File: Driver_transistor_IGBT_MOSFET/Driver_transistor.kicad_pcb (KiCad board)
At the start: 2 copper layers, 79.5 x 34.3 mm, 12 parts, among them J3 Conn_01x02, J4 Conn_01x02, J5 Conn_01x01, Q5 IRF830, Q6 IRF830, Q7 IRG4BC30, T1 1:1

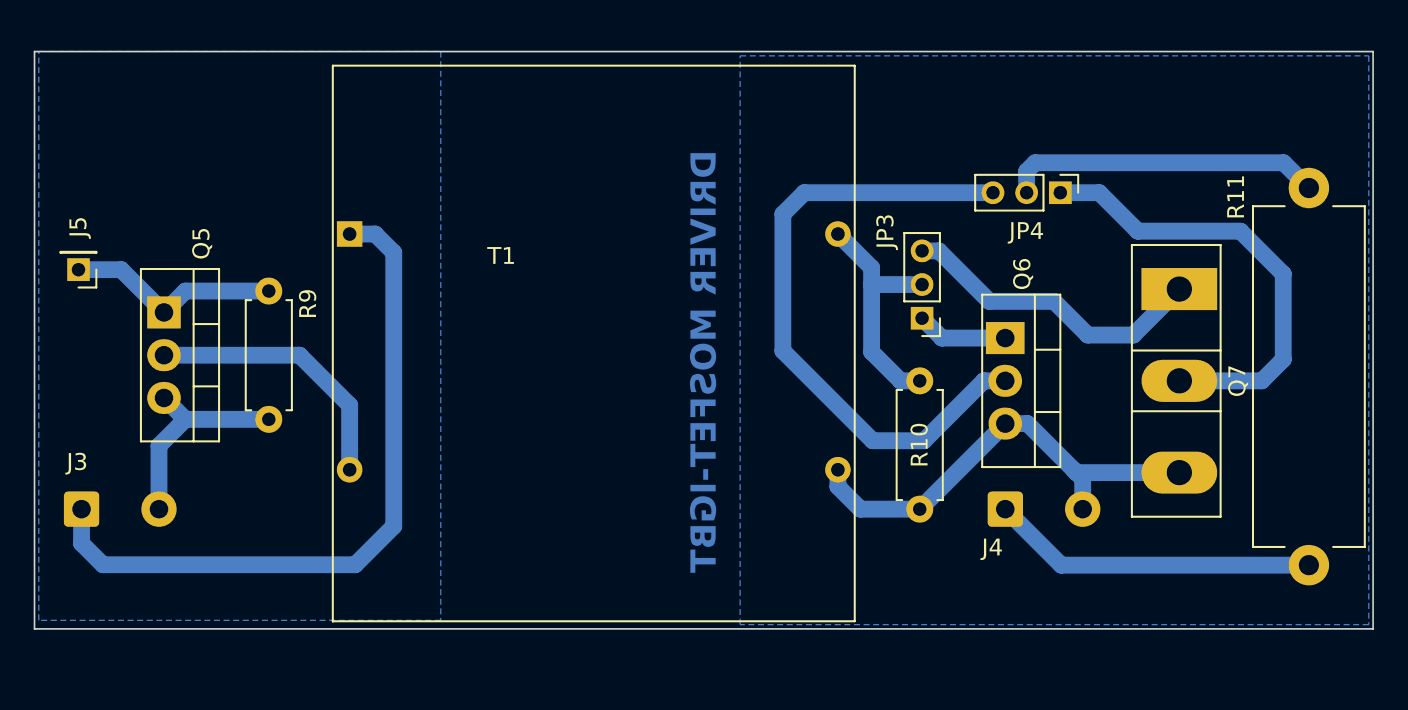
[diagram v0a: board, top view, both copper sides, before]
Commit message: rediseño driver IGBT-MOSFET
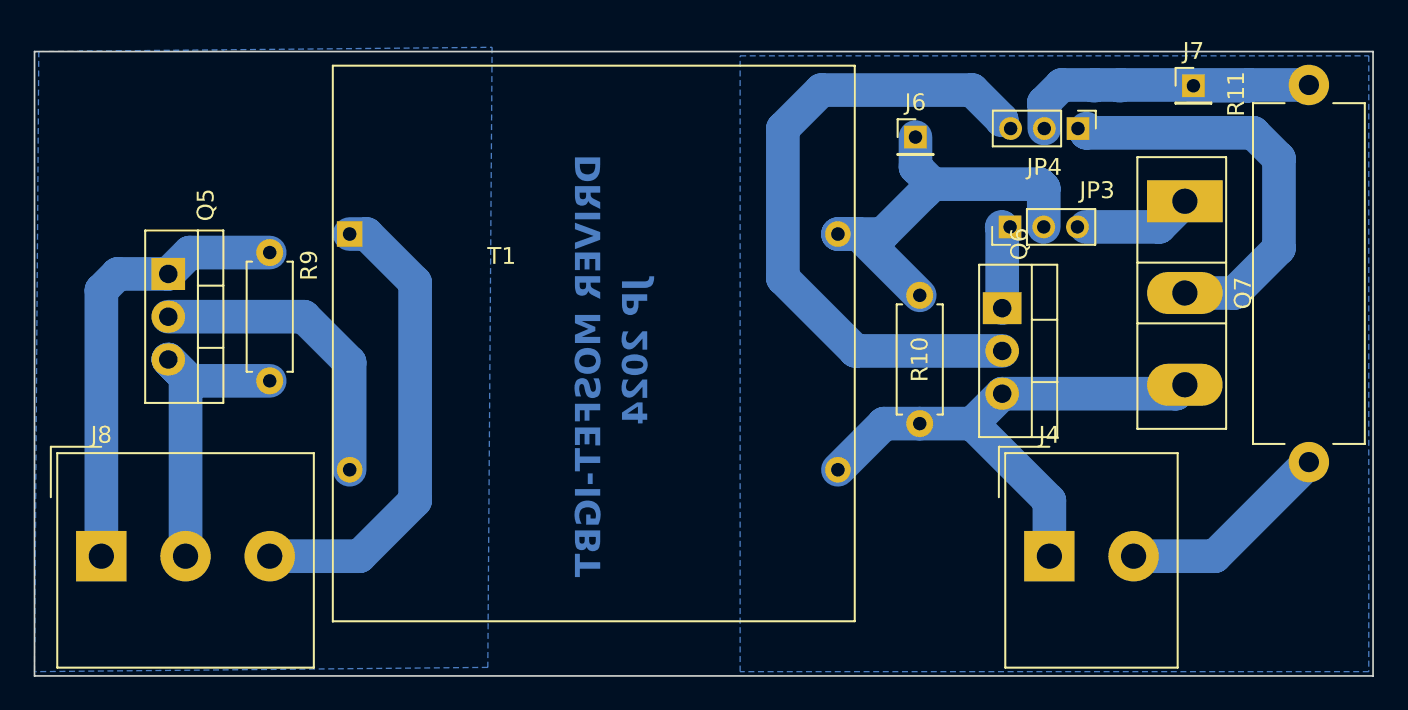
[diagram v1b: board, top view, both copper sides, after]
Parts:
- removed J3: Conn_01x02, Connector_Wire:SolderWire-0.5sqmm_1x02_P4.6mm_D0.9mm_OD2.1mm
- removed J5: Conn_01x01, Connector_PinHeader_2.00mm:PinHeader_1x01_P2.00mm_Vertical
- added J6: gate, Connector_PinHeader_2.00mm:PinHeader_1x01_P2.00mm_Vertical, F.Cu at (149.6, 31.2)
- added J7: drenador, Connector_PinHeader_2.00mm:PinHeader_1x01_P2.00mm_Vertical, F.Cu at (166.1, 28.2)
- added J8: Conn_01x03, TerminalBlock_Altech:Altech_AK300_1x03_P5.00mm_45-Degree, F.Cu at (101.3, 56.1)
- J4: footprint Connector_Wire:SolderWire-0.5sqmm_1x02_P4.6mm_D0.9mm_OD2.1mm -> TerminalBlock_Altech:Altech_AK300_1x02_P5.00mm_45-Degree
- moved JP3 7.53 mm to (155.2, 36.6), turned to 90 degrees
- moved R11 6.12 mm to (173.0, 28.1)
- moved Q7 5.23 mm to (165.6, 35.1)
- moved R10 5.08 mm to (149.9, 48.3)
- moved JP4 3.95 mm to (159.3, 30.7)
- moved J4 3.83 mm to (157.6, 56.1)
- moved Q5 2.30 mm to (105.2, 39.4)
- moved R9 2.29 mm to (111.3, 45.7)
- moved Q6 1.79 mm to (154.8, 41.4)
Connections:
- J4 pad 1: VDD -> GND2
- J4 pad 2: GND2 -> VDD
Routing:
- net pwm1: track 12.9 -> 26.7 mm
- net VCC: track 41.4 -> 28.0 mm
- net Net-(JP3-B): track 18.5 -> 6.51 mm
- net Net-(J6-Pin_1): track 14.4 -> 26.1 mm
- net VDD: track 19.4 -> 12.7 mm
- net GND1: track 12.7 -> 18.7 mm
- net GND2: track 27.5 -> 32.5 mm
- net Net-(JP4-A): track 27.0 -> 24.3 mm
- net Net-(J7-Pin_1): track 18.9 -> 21.2 mm
- net Net-(Q5-D): track 16.1 -> 18.3 mm
- net Net-(JP3-A): track 5.43 -> 4.84 mm
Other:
- board size 79.5 x 34.3 mm -> 79.5 x 37.1 mm
- board text added: "JP 2024"

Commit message: rediseño driver IGBT-MOSFET
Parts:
- moved R11 7.73 mm to (178.3, 33.7)
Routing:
- net Net-(J7-Pin_1): track 21.2 -> 30.6 mm
- net VDD: track 12.7 -> 15.7 mm
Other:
- board size 79.5 x 37.1 mm -> 85.9 x 37.1 mm
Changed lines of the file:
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@@
   )
   (footprint "Resistor_THT:R_Axial_Power_L20.0mm_W6.4mm_P22.40mm" (layer "F.Cu")
-    (at 172.974 28.146 -90)
+    (at 178.308 33.734 -90)
     (descr "Resistor, Axial_Power series, Box, pin pitch=22.4mm, 4W, length*width*height=20*6.4*6.4mm^3, http://cdn-reichelt.de/documents/datenblatt/B400/5WAXIAL_9WAXIAL_11WAXIAL_17WAXIAL%23YAG.pdf")
     (tags "Resistor Axial_Power series Box pin pitch 22.4mm 4W length 20mm width 6.4mm height 6.4mm")
@@
     )
   )
-  (gr_rect (start 97.282 26.162) (end 176.784 63.246)
+  (gr_rect (start 97.282 26.162) (end 183.134 63.246)
     (stroke (width 0.1) (type default)) (fill none) (layer "Edge.Cuts"))
   (gr_text "JP 2024" (at 133.858 39.624 90) (layer "B.Cu")
@@
   (segment (start 111.252 45.72) (end 106.497 45.72) (width 2) (layer "B.Cu") (net 2))
   (segment (start 106.497 45.72) (end 105.227 44.45) (width 2) (layer "B.Cu") (net 2))
-  (segment (start 162.56 56.134) (end 167.386 56.134) (width 2) (layer "B.Cu") (net 3))
-  (segment (start 167.386 56.134) (end 172.974 50.546) (width 2) (layer "B.Cu") (net 3))
+  (segment (start 178.308 56.134) (end 162.56 56.134) (width 2) (layer "B.Cu") (net 3))
   (segment (start 152.979 48.26) (end 154.757 46.482) (width 2) (layer "B.Cu") (net 4))
   (segment (start 157.56 56.134) (end 157.56 52.841) (width 2) (layer "B.Cu") (net 4))
@@
   (segment (start 145 37) (end 147.658 37) (width 2) (layer "B.Cu") (net 11))
   (segment (start 169.418 28.146) (end 161.798 28.146) (width 2) (layer "B.Cu") (net 12))
+  (segment (start 175.72 28.146) (end 178.308 30.734) (width 2) (layer "B.Cu") (net 12))
   (segment (start 166.116 28.194) (end 169.37 28.194) (width 2) (layer "B.Cu") (net 12))
   (segment (start 158.29 28.146) (end 157.226 29.21) (width 2) (layer "B.Cu") (net 12))
-  (segment (start 172.974 28.146) (end 169.418 28.146) (width 2) (layer "B.Cu") (net 12))
   (segment (start 157.226 29.21) (end 157.258 29.242) (width 2) (layer "B.Cu") (net 12))
   (segment (start 161.798 28.146) (end 160.274 28.146) (width 2) (layer "B.Cu") (net 12))
   (segment (start 160.274 28.146) (end 158.29 28.146) (width 2) (layer "B.Cu") (net 12))
+  (segment (start 178.308 30.734) (end 178.308 33.734) (width 2) (layer "B.Cu") (net 12))
   (segment (start 157.258 29.242) (end 157.258 30.734) (width 2) (layer "B.Cu") (net 12))
   (segment (start 161.75 28.194) (end 161.798 28.146) (width 2) (layer "B.Cu") (net 12))
   (segment (start 169.37 28.194) (end 169.418 28.146) (width 2) (layer "B.Cu") (net 12))
   (segment (start 160.226 28.194) (end 160.274 28.146) (width 2) (layer "B.Cu") (net 12))
+  (segment (start 169.418 28.146) (end 175.72 28.146) (width 2) (layer "B.Cu") (net 12))
   (zone (net 2) (net_name "GND1") (layer "B.Cu") (hatch edge 0.5)
     (connect_pads (clearance 2))
@@
     (polygon
       (pts
-        (xy 176.53 26.416)
-        (xy 176.53 62.992)
+        (xy 182.88 26.416)
+        (xy 182.88 62.992)
         (xy 139.192 62.992)
         (xy 139.192 26.416)

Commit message: para vos juan
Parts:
- added J3: surtidor, Connector_PinHeader_2.00mm:PinHeader_1x01_P2.00mm_Vertical, F.Cu at (104.8, 22.7)
- moved J7 76.7 mm to (89.6, 22.7)
- moved R10 76.7 mm to (73.3, 42.8)
- moved J4 76.7 mm to (81.0, 50.7)
- moved JP3 76.7 mm to (78.7, 31.1)
- moved JP4 76.7 mm to (82.7, 25.3)
- moved Q5 76.7 mm to (28.7, 33.9)
- moved Q6 76.7 mm to (78.2, 36.0)
- moved Q7 76.7 mm to (89.1, 29.6)
- moved J6 76.7 mm to (73.1, 25.8)
- moved J8 76.7 mm to (24.7, 50.7)
- moved R11 76.7 mm to (101.8, 28.3)
- moved R9 76.7 mm to (34.7, 40.3)
- moved T1 76.7 mm to (53.5, 36.5)
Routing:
- net GND2: track 32.5 -> 63.9 mm
- net Net-(J7-Pin_1): track 30.6 -> 32.1 mm
